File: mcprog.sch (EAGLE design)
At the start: 53 parts, among them IC1 MCP2210SO, IC2 MCP1703SOT-89, J1 AVRSPI-61.27, J2 AVRSPI-62.56-V, Q1 MOSFET-NCHANNELSMD, X1 MICRO-USB-AB, X2 12MHz

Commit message: board, v1
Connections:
- removed net !RESET!: R3.1, R6.1, R8.1
- removed net !RST_UC!: IC1SPI.GP0, R24.2
- new net !RST_TARGET!: IC1SPI.GP0, R24.2, R3.1, R6.1, R8.1
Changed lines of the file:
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@@
 <segment>
 <pinref part="R1" gate="G$1" pin="1"/>
-<wire x1="157.48" y1="88.9" x2="139.7" y2="88.9" width="0.1524" layer="91"/>
-<label x="142.24" y="88.9" size="1.778" layer="95"/>
+<wire x1="157.48" y1="88.9" x2="132.08" y2="88.9" width="0.1524" layer="91"/>
+<label x="134.62" y="88.9" size="1.778" layer="95"/>
 </segment>
 <segment>
 <pinref part="R4" gate="G$1" pin="1"/>
-<wire x1="157.48" y1="71.12" x2="139.7" y2="71.12" width="0.1524" layer="91"/>
-<label x="142.24" y="71.12" size="1.778" layer="95"/>
+<wire x1="157.48" y1="71.12" x2="132.08" y2="71.12" width="0.1524" layer="91"/>
+<label x="134.62" y="71.12" size="1.778" layer="95"/>
 </segment>
 <segment>
 <pinref part="R10" gate="G$1" pin="1"/>
-<wire x1="157.48" y1="43.18" x2="139.7" y2="43.18" width="0.1524" layer="91"/>
-<label x="142.24" y="43.18" size="1.778" layer="95"/>
+<wire x1="157.48" y1="43.18" x2="132.08" y2="43.18" width="0.1524" layer="91"/>
+<label x="134.62" y="43.18" size="1.778" layer="95"/>
 </segment>
 <segment>
@@
 <segment>
 <pinref part="R2" gate="G$1" pin="1"/>
-<wire x1="154.94" y1="86.36" x2="139.7" y2="86.36" width="0.1524" layer="91"/>
-<label x="142.24" y="86.36" size="1.778" layer="95"/>
+<wire x1="154.94" y1="86.36" x2="132.08" y2="86.36" width="0.1524" layer="91"/>
+<label x="134.62" y="86.36" size="1.778" layer="95"/>
 </segment>
 <segment>
 <pinref part="R5" gate="G$1" pin="1"/>
-<wire x1="152.4" y1="68.58" x2="139.7" y2="68.58" width="0.1524" layer="91"/>
-<label x="142.24" y="68.58" size="1.778" layer="95"/>
+<wire x1="152.4" y1="68.58" x2="132.08" y2="68.58" width="0.1524" layer="91"/>
+<label x="134.62" y="68.58" size="1.778" layer="95"/>
 </segment>
 <segment>
 <pinref part="R9" gate="G$1" pin="1"/>
-<wire x1="152.4" y1="45.72" x2="139.7" y2="45.72" width="0.1524" layer="91"/>
-<label x="142.24" y="45.72" size="1.778" layer="95"/>
+<wire x1="152.4" y1="45.72" x2="132.08" y2="45.72" width="0.1524" layer="91"/>
+<label x="134.62" y="45.72" size="1.778" layer="95"/>
 </segment>
 <segment>
@@
 <wire x1="172.72" y1="142.24" x2="172.72" y2="121.92" width="0.1524" layer="91"/>
 <label x="172.72" y="124.46" size="1.778" layer="95" rot="R90"/>
-</segment>
-</net>
-<net name="!RESET!" class="0">
-<segment>
-<pinref part="R3" gate="G$1" pin="1"/>
-<wire x1="157.48" y1="83.82" x2="139.7" y2="83.82" width="0.1524" layer="91"/>
-<label x="142.24" y="83.82" size="1.778" layer="95"/>
-</segment>
-<segment>
-<pinref part="R6" gate="G$1" pin="1"/>
-<wire x1="157.48" y1="66.04" x2="139.7" y2="66.04" width="0.1524" layer="91"/>
-<label x="142.24" y="66.04" size="1.778" layer="95"/>
-</segment>
-<segment>
-<pinref part="R8" gate="G$1" pin="1"/>
-<wire x1="157.48" y1="48.26" x2="139.7" y2="48.26" width="0.1524" layer="91"/>
-<label x="142.24" y="48.26" size="1.778" layer="95"/>
 </segment>
 </net>
@@
 <segment>
 <pinref part="R7" gate="G$1" pin="1"/>
-<wire x1="157.48" y1="53.34" x2="139.7" y2="53.34" width="0.1524" layer="91"/>
-<label x="142.24" y="53.34" size="1.778" layer="95"/>
+<wire x1="157.48" y1="53.34" x2="132.08" y2="53.34" width="0.1524" layer="91"/>
+<label x="134.62" y="53.34" size="1.778" layer="95"/>
 </segment>
 <segment>
@@
 </segment>
 </net>
-<net name="!RST_UC!" class="0">
-<segment>
-<pinref part="IC1" gate="SPI" pin="GP0"/>
-<wire x1="177.8" y1="142.24" x2="177.8" y2="121.92" width="0.1524" layer="91"/>
-<label x="177.8" y="124.46" size="1.778" layer="95" rot="R90"/>
-</segment>
-<segment>
-<wire x1="218.44" y1="142.24" x2="218.44" y2="119.38" width="0.1524" layer="91"/>
-<pinref part="R24" gate="G$1" pin="2"/>
-<label x="218.44" y="121.92" size="1.778" layer="95" rot="R90"/>
-</segment>
-</net>
 <net name="!SPI_CS!" class="0">
 <segment>
@@
 <segment>
 <pinref part="R13" gate="G$1" pin="1"/>
-<wire x1="152.4" y1="50.8" x2="139.7" y2="50.8" width="0.1524" layer="91"/>
-<label x="142.24" y="50.8" size="1.778" layer="95"/>
+<wire x1="152.4" y1="50.8" x2="132.08" y2="50.8" width="0.1524" layer="91"/>
+<label x="134.62" y="50.8" size="1.778" layer="95"/>
 </segment>
 </net>
@@
 </segment>
 </net>
+<net name="!RST_TARGET!" class="0">
+<segment>
+<pinref part="IC1" gate="SPI" pin="GP0"/>
+<wire x1="177.8" y1="142.24" x2="177.8" y2="121.92" width="0.1524" layer="91"/>
+<label x="177.8" y="124.46" size="1.778" layer="95" rot="R90"/>
+</segment>
+<segment>
+<pinref part="R3" gate="G$1" pin="1"/>
+<wire x1="157.48" y1="83.82" x2="132.08" y2="83.82" width="0.1524" layer="91"/>
+<label x="134.62" y="83.82" size="1.778" layer="95"/>
+</segment>
+<segment>
+<pinref part="R6" gate="G$1" pin="1"/>
+<wire x1="157.48" y1="66.04" x2="132.08" y2="66.04" width="0.1524" layer="91"/>
+<label x="134.62" y="66.04" size="1.778" layer="95"/>
+</segment>
+<segment>
+<pinref part="R8" gate="G$1" pin="1"/>
+<wire x1="157.48" y1="48.26" x2="132.08" y2="48.26" width="0.1524" layer="91"/>
+<label x="134.62" y="48.26" size="1.778" layer="95"/>
+</segment>
+<segment>
+<wire x1="218.44" y1="142.24" x2="218.44" y2="119.38" width="0.1524" layer="91"/>
+<pinref part="R24" gate="G$1" pin="2"/>
+<label x="218.44" y="121.92" size="1.778" layer="95" rot="R90"/>
+</segment>
+</net>

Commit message: v1.0
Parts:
- removed LOGO1: (no value), bytewerk-logo:BWLOGO
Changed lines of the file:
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@@
 <part name="LED2" library="bytewerk-led" deviceset="LED0603" device=""/>
 <part name="LED3" library="bytewerk-led" deviceset="LED0603" device=""/>
-<part name="LOGO1" library="bytewerk-logo" deviceset="BWLOGO" device=""/>
 <part name="C1" library="bytewerk-passive" deviceset="C" device="0603" value="100nF/10V"/>
 <part name="C2" library="bytewerk-passive" deviceset="C" device="1206" value="22uF/10V"/>
@@
 <instance part="LED2" gate="G$1" x="251.46" y="60.96" rot="R270"/>
 <instance part="LED3" gate="G$1" x="213.36" y="137.16" rot="R270"/>
-<instance part="LOGO1" gate="G$1" x="180.34" y="10.16"/>
 <instance part="C1" gate="G$1" x="73.66" y="86.36" rot="R90"/>
 <instance part="C2" gate="G$1" x="78.74" y="86.36" rot="R90"/>

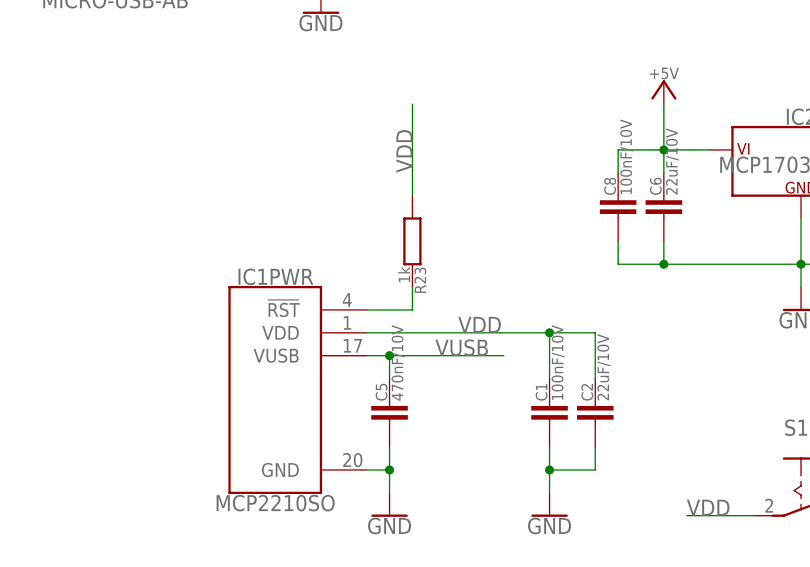
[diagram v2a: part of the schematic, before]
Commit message: Fixing some minor DRC problems. R23 now is 10k
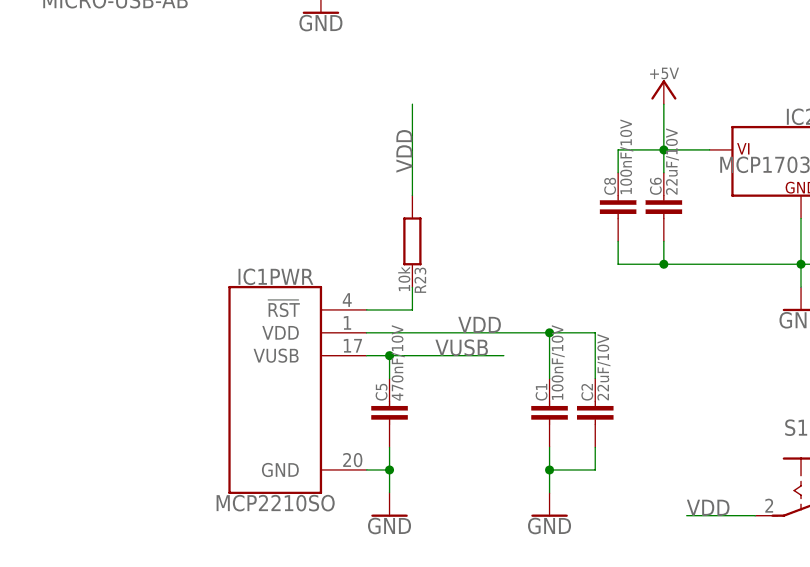
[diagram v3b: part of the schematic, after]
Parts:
- R23: value 1k -> 10k
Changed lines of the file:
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@@
 <part name="D1" library="bytewerk-passive" deviceset="1N5819HW" device=""/>
 <part name="C5" library="bytewerk-passive" deviceset="C" device="0603" value="470nF/10V"/>
-<part name="R23" library="bytewerk-passive" deviceset="R" device="0603" value="1k"/>
+<part name="R23" library="bytewerk-passive" deviceset="R" device="0603" value="10k"/>
 <part name="IC2" library="bytewerk-vreg" deviceset="MCP1703" device="SOT-89"/>
 <part name="U$13" library="bytewerk-symbol" deviceset="GND" device=""/>
@@
 </sheet>
 </sheets>
+<errors>
+</errors>
 </schematic>
 </drawing>

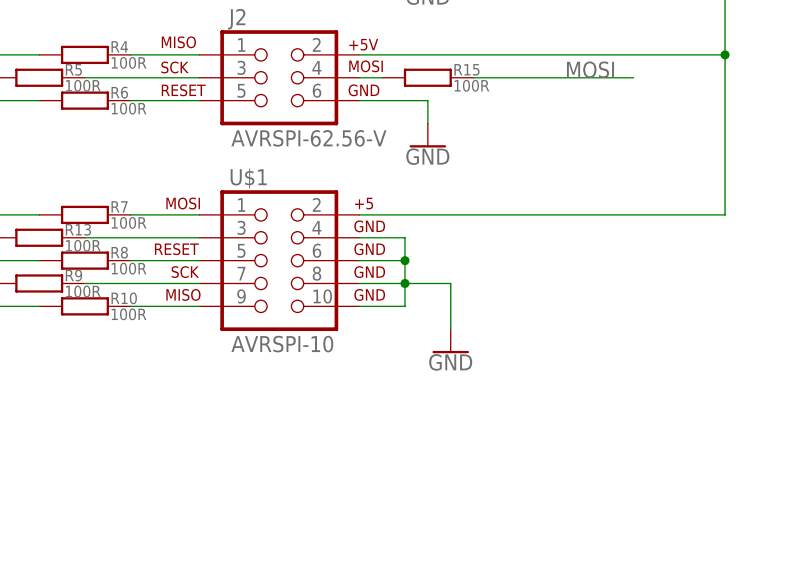
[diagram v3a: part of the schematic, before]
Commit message: improve GND path
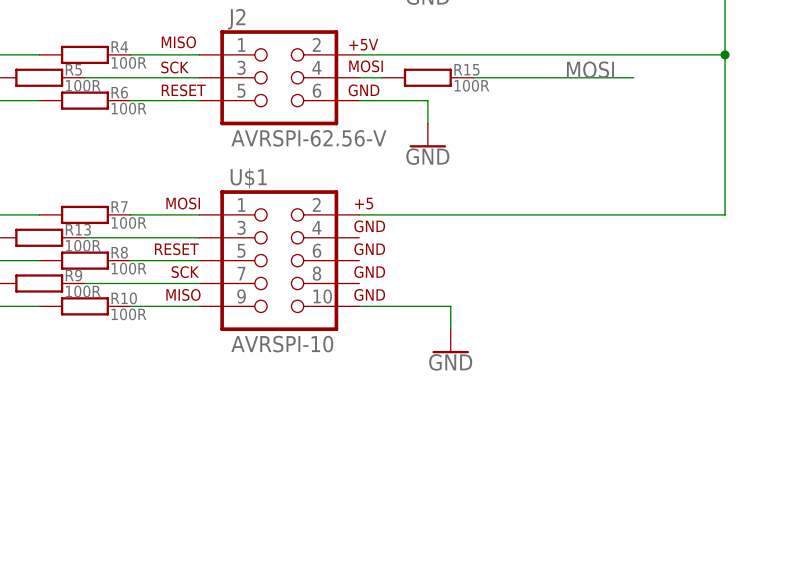
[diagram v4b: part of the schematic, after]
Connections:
- net GND: no longer U$1.4, U$1.6, U$1.8
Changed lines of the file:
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@@
-</segment>
-<segment>
-<pinref part="U$1" gate="A" pin="4"/>
-<wire x1="193.04" y1="50.8" x2="198.12" y2="50.8" width="0.1524" layer="91"/>
-<wire x1="198.12" y1="50.8" x2="198.12" y2="48.26" width="0.1524" layer="91"/>
-<pinref part="U$1" gate="A" pin="10"/>
-<wire x1="198.12" y1="48.26" x2="198.12" y2="45.72" width="0.1524" layer="91"/>
-<wire x1="198.12" y1="45.72" x2="198.12" y2="43.18" width="0.1524" layer="91"/>
-<wire x1="198.12" y1="43.18" x2="193.04" y2="43.18" width="0.1524" layer="91"/>
-<pinref part="U$1" gate="A" pin="8"/>
-<wire x1="193.04" y1="45.72" x2="198.12" y2="45.72" width="0.1524" layer="91"/>
-<junction x="198.12" y="45.72"/>
-<pinref part="U$1" gate="A" pin="6"/>
-<wire x1="193.04" y1="48.26" x2="198.12" y2="48.26" width="0.1524" layer="91"/>
-<junction x="198.12" y="48.26"/>
-<pinref part="U$5" gate="G$1" pin="GND"/>
-<wire x1="198.12" y1="45.72" x2="203.2" y2="45.72" width="0.1524" layer="91"/>
-<wire x1="203.2" y1="45.72" x2="203.2" y2="40.64" width="0.1524" layer="91"/>
 </segment>
 <segment>
@@
 <junction x="71.12" y="17.78"/>
 </segment>
+<segment>
+<pinref part="U$1" gate="A" pin="10"/>
+<pinref part="U$5" gate="G$1" pin="GND"/>
+<wire x1="193.04" y1="43.18" x2="203.2" y2="43.18" width="0.1524" layer="91"/>
+<wire x1="203.2" y1="43.18" x2="203.2" y2="40.64" width="0.1524" layer="91"/>
+</segment>
 </net>

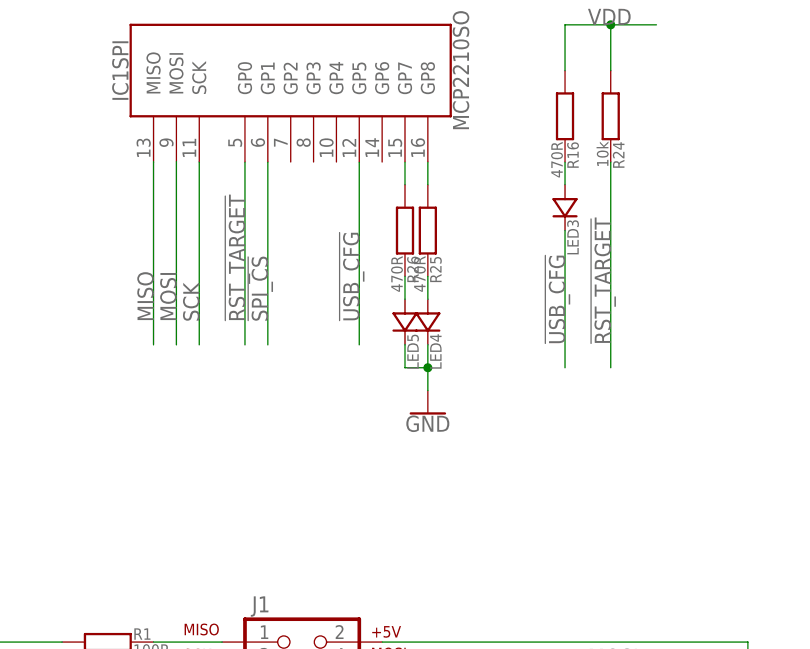
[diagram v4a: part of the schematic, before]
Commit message: attach PROG led to GPIO6 instead of GPIO8 GPIO8 refused to be an output for some unknown reason
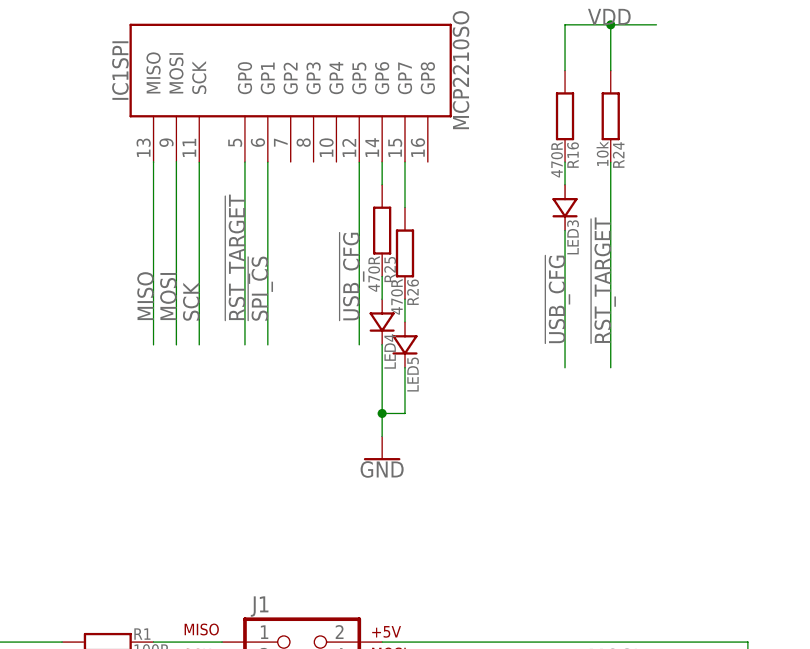
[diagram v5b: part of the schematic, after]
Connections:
- removed net N$30: IC1SPI.GP8, R25.1
- new net N$16: IC1SPI.GP6, R25.1
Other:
- moved on the sheet: LED4, LED5, R25, R26
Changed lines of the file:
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@@
 <?xml version="1.0" encoding="utf-8"?>
 <!DOCTYPE eagle SYSTEM "eagle.dtd">
-<eagle version="6.5.0">
+<eagle version="6.6.0">
 <drawing>
 <settings>
@@
 <instance part="R24" gate="G$1" x="218.44" y="147.32" rot="R270"/>
 <instance part="U$2" gate="G$1" x="73.66" y="73.66"/>
-<instance part="LED4" gate="G$1" x="198.12" y="124.46" rot="R270"/>
-<instance part="R25" gate="G$1" x="198.12" y="134.62" rot="R270"/>
-<instance part="U$3" gate="G$1" x="198.12" y="114.3"/>
-<instance part="R26" gate="G$1" x="195.58" y="134.62" rot="R270"/>
-<instance part="LED5" gate="G$1" x="195.58" y="124.46" rot="R270"/>
+<instance part="LED4" gate="G$1" x="193.04" y="124.46" rot="R270"/>
+<instance part="R25" gate="G$1" x="193.04" y="134.62" rot="R270"/>
+<instance part="U$3" gate="G$1" x="193.04" y="109.22"/>
+<instance part="R26" gate="G$1" x="195.58" y="132.08" rot="R270"/>
+<instance part="LED5" gate="G$1" x="195.58" y="121.92" rot="R270"/>
 <instance part="S1" gate="1" x="101.6" y="76.2" rot="R270"/>
 <instance part="U$4" gate="G$1" x="114.3" y="81.28"/>
@@
 <pinref part="U$3" gate="G$1" pin="GND"/>
 <pinref part="LED4" gate="G$1" pin="C"/>
-<wire x1="198.12" y1="116.84" x2="198.12" y2="119.38" width="0.1524" layer="91"/>
+<wire x1="193.04" y1="111.76" x2="193.04" y2="114.3" width="0.1524" layer="91"/>
 <pinref part="LED5" gate="G$1" pin="C"/>
-<wire x1="198.12" y1="119.38" x2="198.12" y2="121.92" width="0.1524" layer="91"/>
-<wire x1="195.58" y1="121.92" x2="195.58" y2="119.38" width="0.1524" layer="91"/>
-<wire x1="195.58" y1="119.38" x2="198.12" y2="119.38" width="0.1524" layer="91"/>
-<junction x="198.12" y="119.38"/>
+<wire x1="193.04" y1="114.3" x2="193.04" y2="121.92" width="0.1524" layer="91"/>
+<wire x1="195.58" y1="119.38" x2="195.58" y2="114.3" width="0.1524" layer="91"/>
+<wire x1="195.58" y1="114.3" x2="193.04" y2="114.3" width="0.1524" layer="91"/>
+<junction x="193.04" y="114.3"/>
 </segment>
 <segment>
@@
 <pinref part="R25" gate="G$1" pin="2"/>
 <pinref part="LED4" gate="G$1" pin="A"/>
-<wire x1="198.12" y1="129.54" x2="198.12" y2="127" width="0.1524" layer="91"/>
-</segment>
-</net>
-<net name="N$30" class="0">
-<segment>
-<pinref part="R25" gate="G$1" pin="1"/>
-<pinref part="IC1" gate="SPI" pin="GP8"/>
-<wire x1="198.12" y1="139.7" x2="198.12" y2="142.24" width="0.1524" layer="91"/>
+<wire x1="193.04" y1="129.54" x2="193.04" y2="127" width="0.1524" layer="91"/>
 </segment>
 </net>
@@
 <pinref part="LED5" gate="G$1" pin="A"/>
 <pinref part="R26" gate="G$1" pin="2"/>
-<wire x1="195.58" y1="127" x2="195.58" y2="129.54" width="0.1524" layer="91"/>
+<wire x1="195.58" y1="124.46" x2="195.58" y2="127" width="0.1524" layer="91"/>
 </segment>
 </net>
@@
 <pinref part="R26" gate="G$1" pin="1"/>
 <pinref part="IC1" gate="SPI" pin="GP7"/>
-<wire x1="195.58" y1="139.7" x2="195.58" y2="142.24" width="0.1524" layer="91"/>
+<wire x1="195.58" y1="137.16" x2="195.58" y2="142.24" width="0.1524" layer="91"/>
 </segment>
 </net>
@@
 </segment>
 </net>
+<net name="N$16" class="0">
+<segment>
+<pinref part="IC1" gate="SPI" pin="GP6"/>
+<pinref part="R25" gate="G$1" pin="1"/>
+<wire x1="193.04" y1="142.24" x2="193.04" y2="139.7" width="0.1524" layer="91"/>
+</segment>
+</net>
